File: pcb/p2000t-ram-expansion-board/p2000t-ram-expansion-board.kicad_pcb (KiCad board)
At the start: 2 copper layers, 110 x 68.1 mm, 28 parts, among them J1 EXPANSION BOARD, J2 POWER, J3 TERMINAL, U1 74HC04, U2 CY62256-70PC, U3 74HC00, U4 CY62256-70PC, U5 74HC688, U6 74HC32, U7 74HC173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

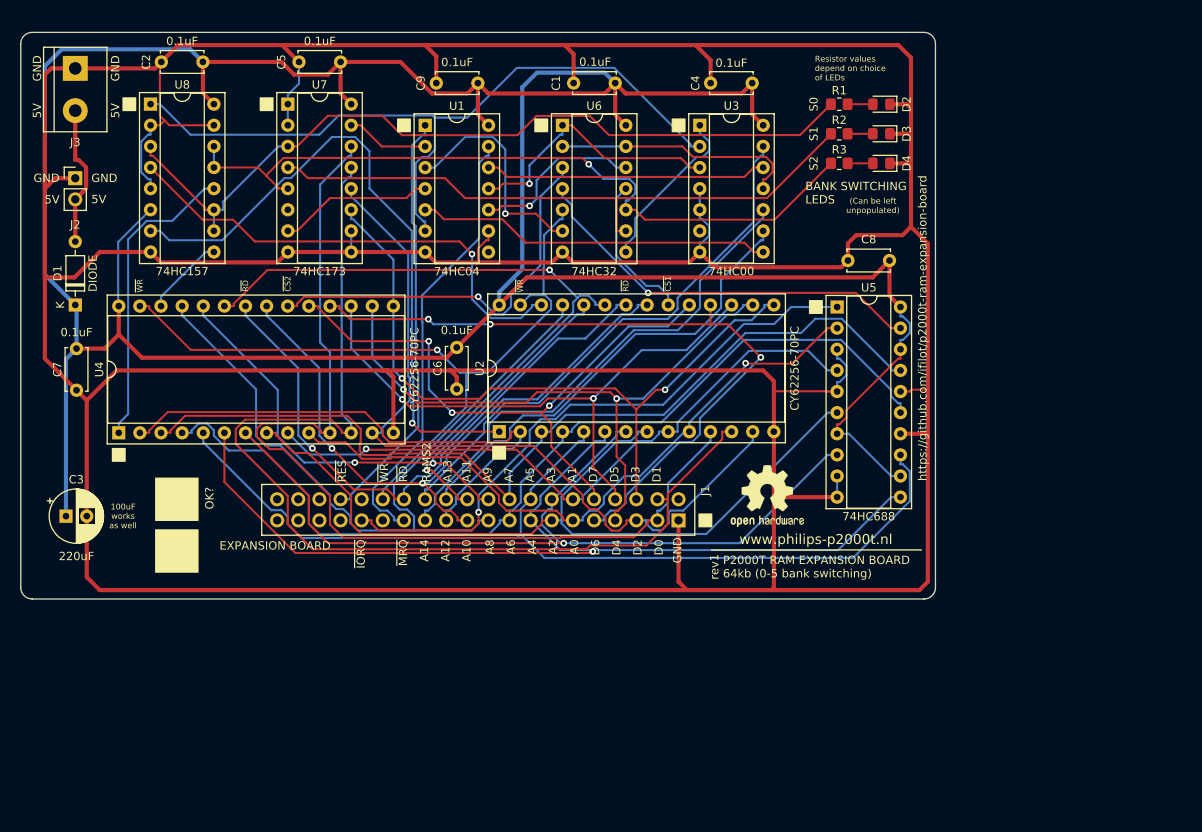
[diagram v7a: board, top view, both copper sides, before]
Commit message: Adding 74HC245
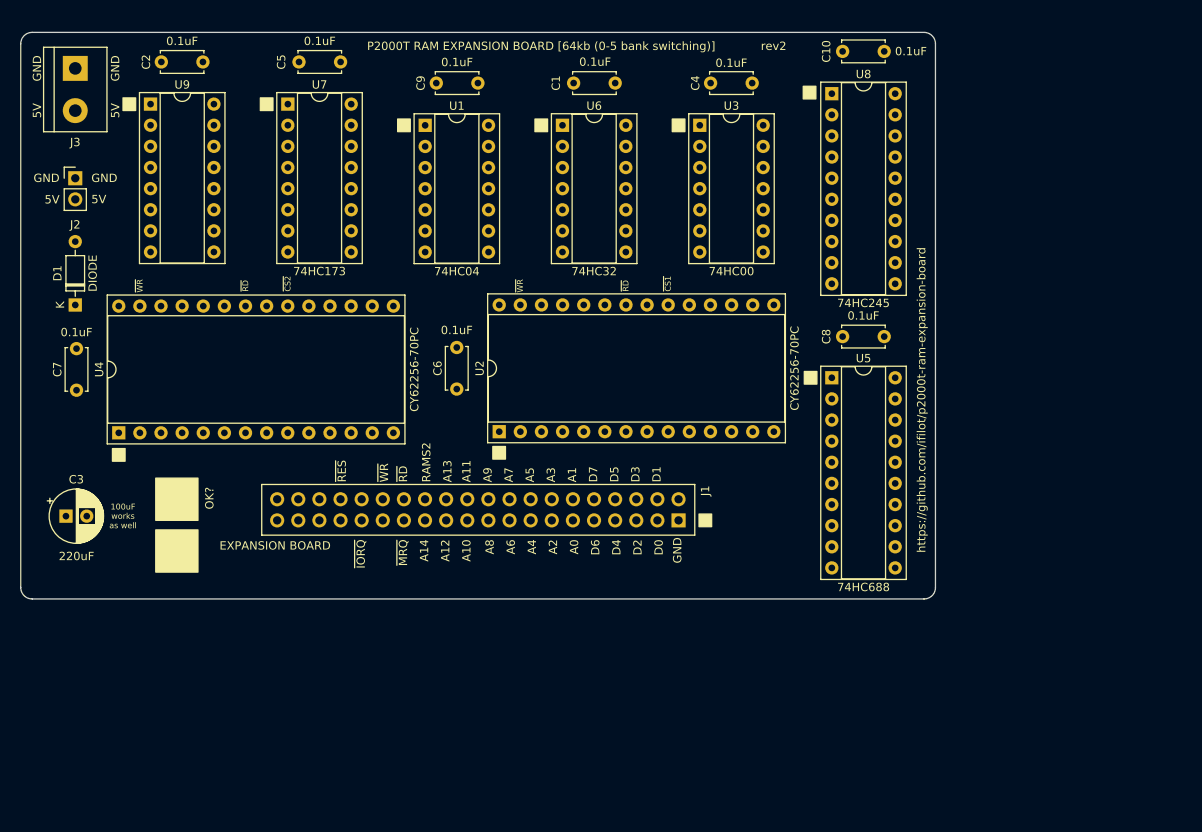
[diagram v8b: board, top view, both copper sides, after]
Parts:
- removed D2, D3, D4: LED, LED_SMD:LED_0805_2012Metric_Pad1.15x1.40mm_HandSolder
- removed R1, R2, R3: R, Resistor_SMD:R_0805_2012Metric_Pad1.20x1.40mm_HandSolder
- removed REF**: OSHW-Logo2_9.8x8mm_SilkScreen, Symbol:OSHW-Logo2_9.8x8mm_SilkScreen
- added C10: 0.1uF, Capacitor_THT:C_Disc_D5.0mm_W2.5mm_P5.00mm, F.Cu at (118.8, 24.1)
- added U9: 74HC157, Package_DIP:DIP-16_W7.62mm_Socket, F.Cu at (35.6, 30.5)
- U8: value 74HC157 -> 74HC245; footprint Package_DIP:DIP-16_W7.62mm_Socket -> Package_DIP:DIP-20_W7.62mm_Socket
- moved U8 81.9 mm to (117.5, 29.2)
- moved C8 9.17 mm to (123.8, 58.4)
- moved U5 8.53 mm to (117.5, 63.4)
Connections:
- U1 pad 11: Net-(U1-Pad11) -> ~{REN}
- U3 pad 3: Net-(U1-Pad11) -> Net-(U3-Pad3)
- U3 pad 4: GND -> Net-(U3-Pad3)
- U3 pad 5: GND -> Net-(U1-Pad10)
- U3 pad 6: unconnected-(U3-Pad6) -> ~{CS1}
- U5 pad 19: Net-(U5-Pad19) -> ~{P=Q}
- U6 pad 1: Net-(U1-Pad11) -> Net-(U3-Pad3)
- U6 pad 11: ~{CS1} -> Net-(U6-Pad11)
- U6 pad 12: Net-(U1-Pad10) -> ~{RD}
- U6 pad 13: ~{REN} -> ~{P=Q}
- U6 pad 4: Net-(U5-Pad19) -> ~{P=Q}
- U7 pad 6: unconnected-(U7-Pad6) -> S3
- U8 pad 1: EO -> +5V
- U8 pad 10: S0 -> GND
- U8 pad 11: S0 -> D7
- U8 pad 12: A14_2 -> D6
- U8 pad 13: S2 -> D5
- U8 pad 14: S2 -> D4
- U8 pad 15: GND -> D3
- U8 pad 16: +5V -> D2
- U8 pad 2: GND -> S0
- U8 pad 3: S0 -> S1
- U8 pad 4: A13_1 -> S2
- U8 pad 5: GND -> S3
- U8 pad 6: +5V -> GND
- U8 pad 7: A14_1 -> GND
- U8 pad 9: A13_2 -> GND
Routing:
- net GND: track 686.8 -> 0.00 mm
- net +5V: track 372.8 -> 0.00 mm
- net D1: track 126.6 -> 0.00 mm
- net A4: track 117.8 -> 0.00 mm, vias 1 -> 0
- net A5: track 117.6 -> 0.00 mm
- net D0: track 117.1 -> 0.00 mm
- net A6: track 112.4 -> 0.00 mm
- net A7: track 110.3 -> 0.00 mm
- net A3: track 103.1 -> 0.00 mm, vias 1 -> 0
- net A2: track 100.1 -> 0.00 mm
- net S0: track 98.0 -> 0.00 mm
- net D2: track 94.2 -> 0.00 mm
- net ~{WR}: track 92.3 -> 0.00 mm, vias 1 -> 0
- net EO: track 90.8 -> 0.00 mm
- net A8: track 90.7 -> 0.00 mm
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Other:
- board text added: "P2000T RAM EXPANSION BOARD [64kb (0-5 bank switching)]"
- board text added: "rev2"
- board text removed: "(Can be left unpopulated)"
- board text removed: "BANK SWITCHING LEDS"
- board text removed: "Resistor values depend on choice of LEDs"
- board text removed: "S0"
- board text removed: "S1"
- board text removed: "S2"
- board text removed: "rev1"
